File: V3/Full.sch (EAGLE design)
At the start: 236 parts, among them X1 SSW-103-02-G-S

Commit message: Commit xD
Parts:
- CLOCK: value (none) -> Yellow
- RESET_PC, RESET_REGS: value (none) -> NORM-OFF
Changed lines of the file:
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@@
 <part name="R2" library="rcl" library_urn="urn:adsk.eagle:library:334" deviceset="R-US_" device="0204/7" package3d_urn="urn:adsk.eagle:package:23498/2" value="1k"/>
 <part name="R5" library="rcl" library_urn="urn:adsk.eagle:library:334" deviceset="R-US_" device="0204/7" package3d_urn="urn:adsk.eagle:package:23498/2" value="~220"/>
-<part name="CLOCK" library="led" library_urn="urn:adsk.eagle:library:259" deviceset="LED" device="5MM" package3d_urn="urn:adsk.eagle:package:15799/2"/>
+<part name="CLOCK" library="led" library_urn="urn:adsk.eagle:library:259" deviceset="LED" device="5MM" package3d_urn="urn:adsk.eagle:package:15799/2" value="Yellow"/>
 <part name="GND2" library="supply1" library_urn="urn:adsk.eagle:library:371" deviceset="GND" device=""/>
 <part name="C2" library="rcl" library_urn="urn:adsk.eagle:library:334" deviceset="CPOL-EU" device="E2-5" package3d_urn="urn:adsk.eagle:package:23346/2" value="0.1uF"/>
@@
 <part name="R80" library="rcl" library_urn="urn:adsk.eagle:library:334" deviceset="R-US_" device="0204/7" package3d_urn="urn:adsk.eagle:package:23498/2" value="~220"/>
 <part name="P+32" library="supply1" library_urn="urn:adsk.eagle:library:371" deviceset="VCC" device=""/>
-<part name="RESET_PC" library="switch-omron" library_urn="urn:adsk.eagle:library:377" deviceset="10-XX" device="" package3d_urn="urn:adsk.eagle:package:27496/1"/>
-<part name="RESET_REGS" library="switch-omron" library_urn="urn:adsk.eagle:library:377" deviceset="10-XX" device="" package3d_urn="urn:adsk.eagle:package:27496/1"/>
+<part name="RESET_PC" library="switch-omron" library_urn="urn:adsk.eagle:library:377" deviceset="10-XX" device="" package3d_urn="urn:adsk.eagle:package:27496/1" value="NORM-OFF"/>
+<part name="RESET_REGS" library="switch-omron" library_urn="urn:adsk.eagle:library:377" deviceset="10-XX" device="" package3d_urn="urn:adsk.eagle:package:27496/1" value="NORM-OFF"/>
 <part name="R81" library="rcl" library_urn="urn:adsk.eagle:library:334" deviceset="R-US_" device="0204/7" package3d_urn="urn:adsk.eagle:package:23498/2" value="~220"/>
 <part name="GND44" library="supply1" library_urn="urn:adsk.eagle:library:371" deviceset="GND" device=""/>

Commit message: Tidy and added Instructions
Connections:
- new net N$232: ADDER_UPPERA.C4, XOR_GATE_2D.I0
- net CTRL_SIG_12: now also XOR_GATE_2D.I1
- net OVERFLOW_FLAG: now also XOR_GATE_2D.O; no longer ADDER_UPPERA.C4
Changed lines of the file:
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@@
 <instance part="NOT_GATE1" gate="A" x="302.26" y="-30.48" smashed="yes" rot="R270"/>
 <instance part="NOT_GATE5_" gate="A" x="619.76" y="218.44" smashed="yes" rot="R180"/>
+<instance part="XOR_GATE_2" gate="D" x="294.64" y="210.82" smashed="yes" rot="R270"/>
 </instances>
 <busses>
@@
 <net name="OVERFLOW_FLAG" class="0">
 <segment>
-<pinref part="ADDER_UPPER" gate="A" pin="C4"/>
-<wire x1="289.56" y1="-17.78" x2="289.56" y2="246.38" width="0.1524" layer="91"/>
-<wire x1="289.56" y1="246.38" x2="381" y2="246.38" width="0.1524" layer="91"/>
+<wire x1="274.32" y1="-17.78" x2="289.56" y2="-17.78" width="0.1524" layer="91"/>
 <wire x1="289.56" y1="-17.78" x2="322.58" y2="-17.78" width="0.1524" layer="91"/>
 <wire x1="322.58" y1="-17.78" x2="322.58" y2="-35.56" width="0.1524" layer="91"/>
@@
 <wire x1="274.32" y1="-48.26" x2="231.14" y2="-48.26" width="0.1524" layer="91"/>
 <pinref part="OVERFLOW_FLAG" gate="G$1" pin="A"/>
-<wire x1="274.32" y1="-17.78" x2="289.56" y2="-17.78" width="0.1524" layer="91"/>
 <wire x1="274.32" y1="-17.78" x2="274.32" y2="-48.26" width="0.1524" layer="91"/>
 <junction x="274.32" y="-17.78"/>
-<junction x="289.56" y="-17.78"/>
 <pinref part="AND_GATE3_" gate="D" pin="I1"/>
+<pinref part="XOR_GATE_2" gate="D" pin="O"/>
+<wire x1="294.64" y1="203.2" x2="294.64" y2="195.58" width="0.1524" layer="91"/>
+<wire x1="294.64" y1="195.58" x2="289.56" y2="195.58" width="0.1524" layer="91"/>
+<wire x1="289.56" y1="195.58" x2="289.56" y2="-17.78" width="0.1524" layer="91"/>
+<junction x="289.56" y="-17.78"/>
 </segment>
 </net>
@@
 <junction x="287.02" y="314.96"/>
 <pinref part="ADDER_LOWER" gate="A" pin="C0"/>
-<wire x1="287.02" y1="297.18" x2="287.02" y2="109.22" width="0.1524" layer="91"/>
+<wire x1="287.02" y1="297.18" x2="287.02" y2="218.44" width="0.1524" layer="91"/>
+<wire x1="287.02" y1="218.44" x2="287.02" y2="109.22" width="0.1524" layer="91"/>
 <wire x1="416.56" y1="271.78" x2="416.56" y2="297.18" width="0.1524" layer="91"/>
 <wire x1="416.56" y1="297.18" x2="287.02" y2="297.18" width="0.1524" layer="91"/>
 <junction x="287.02" y="297.18"/>
+<pinref part="XOR_GATE_2" gate="D" pin="I1"/>
+<wire x1="292.1" y1="218.44" x2="287.02" y2="218.44" width="0.1524" layer="91"/>
+<junction x="287.02" y="218.44"/>
 </segment>
 </net>
@@
 </segment>
 </net>
+<net name="N$232" class="0">
+<segment>
+<pinref part="ADDER_UPPER" gate="A" pin="C4"/>
+<pinref part="XOR_GATE_2" gate="D" pin="I0"/>
+<wire x1="297.18" y1="246.38" x2="381" y2="246.38" width="0.1524" layer="91"/>
+<wire x1="297.18" y1="218.44" x2="297.18" y2="246.38" width="0.1524" layer="91"/>
+</segment>
+</net>

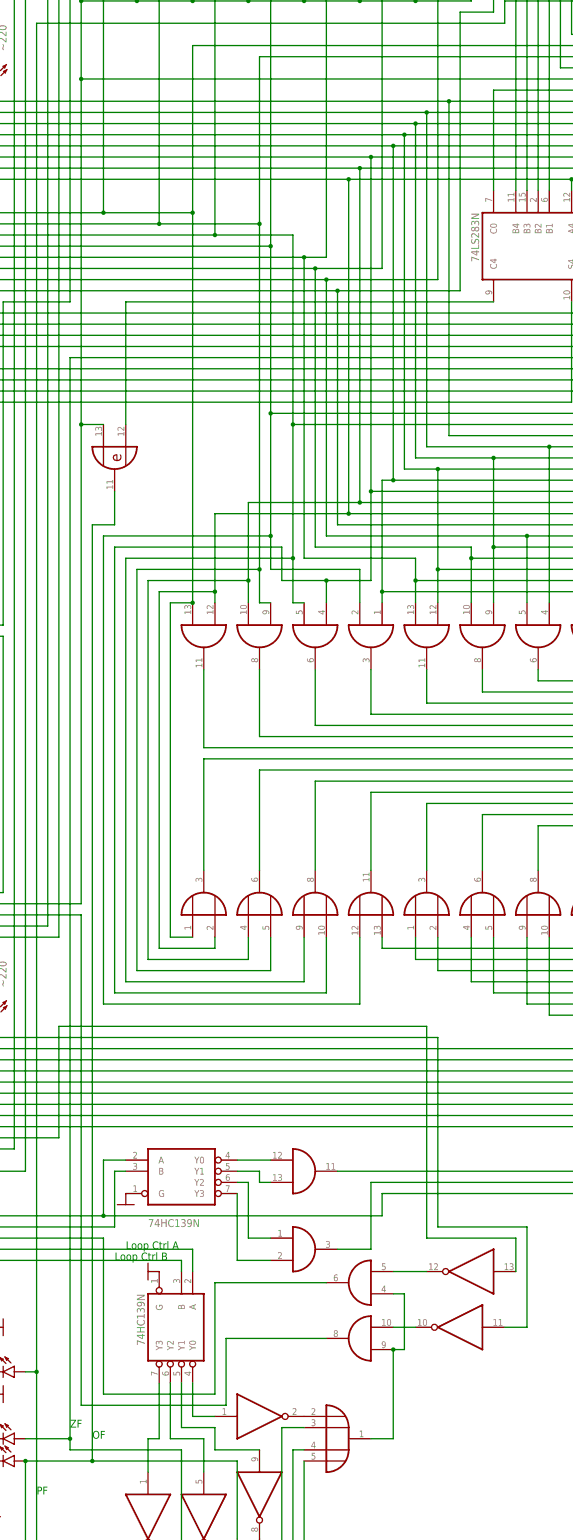
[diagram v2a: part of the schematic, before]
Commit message: Updated spreadsheet and overwritten XOR gate for overflow on subtract
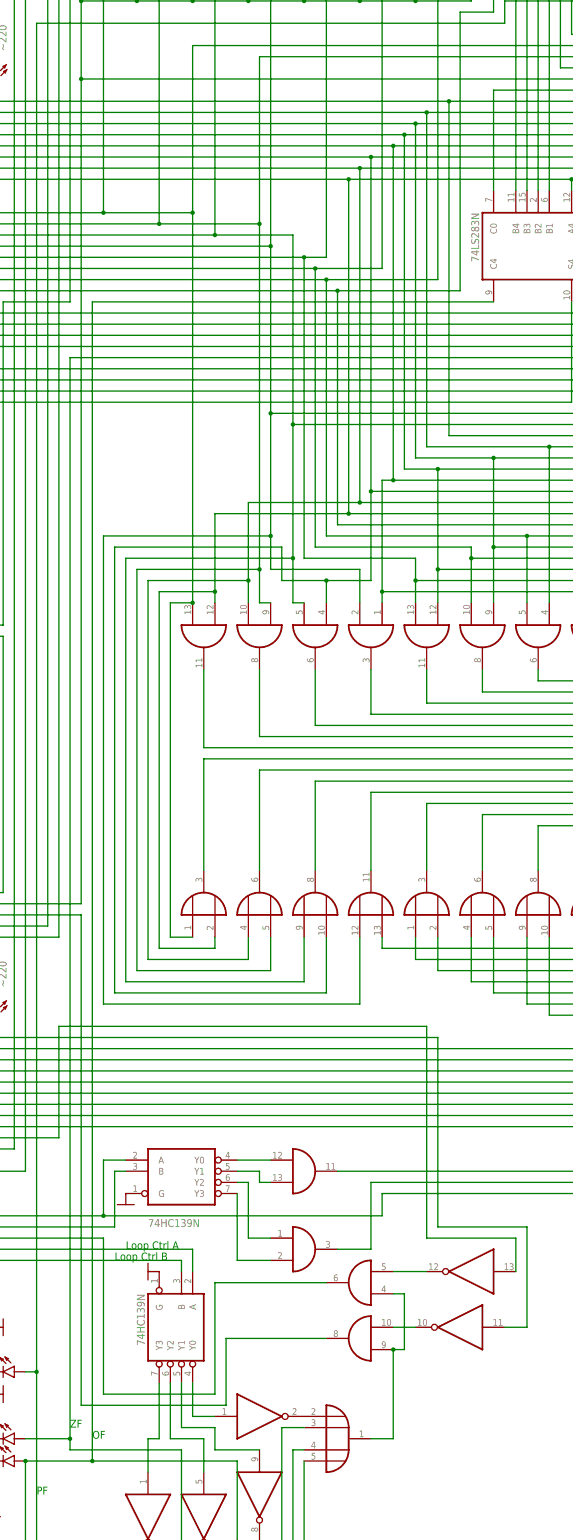
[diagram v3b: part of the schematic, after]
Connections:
- removed net N$232: ADDER_UPPERA.C4, XOR_GATE_2D.I0
- net CTRL_SIG_12: no longer XOR_GATE_2D.I1
- net OVERFLOW_FLAG: now also ADDER_UPPERA.C4; no longer XOR_GATE_2D.O
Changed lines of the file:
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@@
 <instance part="NOT_GATE1" gate="A" x="302.26" y="-30.48" smashed="yes" rot="R270"/>
 <instance part="NOT_GATE5_" gate="A" x="619.76" y="218.44" smashed="yes" rot="R180"/>
-<instance part="XOR_GATE_2" gate="D" x="294.64" y="210.82" smashed="yes" rot="R270"/>
 </instances>
 <busses>
@@
 <junction x="274.32" y="-17.78"/>
 <pinref part="AND_GATE3_" gate="D" pin="I1"/>
-<pinref part="XOR_GATE_2" gate="D" pin="O"/>
-<wire x1="294.64" y1="203.2" x2="294.64" y2="195.58" width="0.1524" layer="91"/>
-<wire x1="294.64" y1="195.58" x2="289.56" y2="195.58" width="0.1524" layer="91"/>
-<wire x1="289.56" y1="195.58" x2="289.56" y2="-17.78" width="0.1524" layer="91"/>
+<wire x1="289.56" y1="246.38" x2="289.56" y2="-17.78" width="0.1524" layer="91"/>
 <junction x="289.56" y="-17.78"/>
+<pinref part="ADDER_UPPER" gate="A" pin="C4"/>
+<wire x1="289.56" y1="246.38" x2="381" y2="246.38" width="0.1524" layer="91"/>
 </segment>
 </net>
@@
 <junction x="287.02" y="314.96"/>
 <pinref part="ADDER_LOWER" gate="A" pin="C0"/>
-<wire x1="287.02" y1="297.18" x2="287.02" y2="218.44" width="0.1524" layer="91"/>
-<wire x1="287.02" y1="218.44" x2="287.02" y2="109.22" width="0.1524" layer="91"/>
+<wire x1="287.02" y1="297.18" x2="287.02" y2="109.22" width="0.1524" layer="91"/>
 <wire x1="416.56" y1="271.78" x2="416.56" y2="297.18" width="0.1524" layer="91"/>
 <wire x1="416.56" y1="297.18" x2="287.02" y2="297.18" width="0.1524" layer="91"/>
 <junction x="287.02" y="297.18"/>
-<pinref part="XOR_GATE_2" gate="D" pin="I1"/>
-<wire x1="292.1" y1="218.44" x2="287.02" y2="218.44" width="0.1524" layer="91"/>
-<junction x="287.02" y="218.44"/>
 </segment>
 </net>
@@
 </segment>
 </net>
-<net name="N$232" class="0">
-<segment>
-<pinref part="ADDER_UPPER" gate="A" pin="C4"/>
-<pinref part="XOR_GATE_2" gate="D" pin="I0"/>
-<wire x1="297.18" y1="246.38" x2="381" y2="246.38" width="0.1524" layer="91"/>
-<wire x1="297.18" y1="218.44" x2="297.18" y2="246.38" width="0.1524" layer="91"/>
-</segment>
-</net>
